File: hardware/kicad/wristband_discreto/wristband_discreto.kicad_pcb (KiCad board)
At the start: 2 copper layers, 32 x 32 mm, 24 parts, among them J1 Battery_Negative_Contact, U1 QFN-32-1EP_5x5mm_P0.5mm_EP3.6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, X1 Crystal_SMD_2016-4Pin_2.0x1.6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

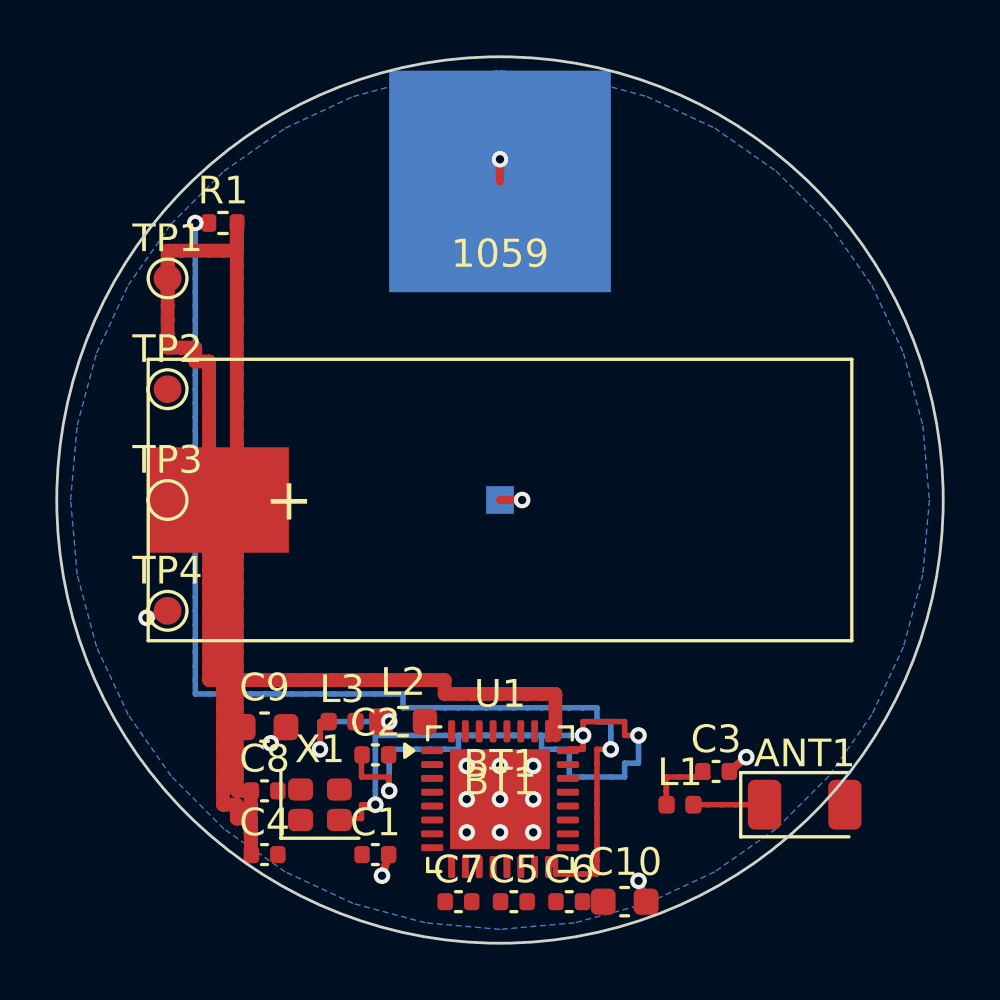
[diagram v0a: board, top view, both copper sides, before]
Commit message: Layouts finish, BM832A migration, fab package, quote, docs and status report
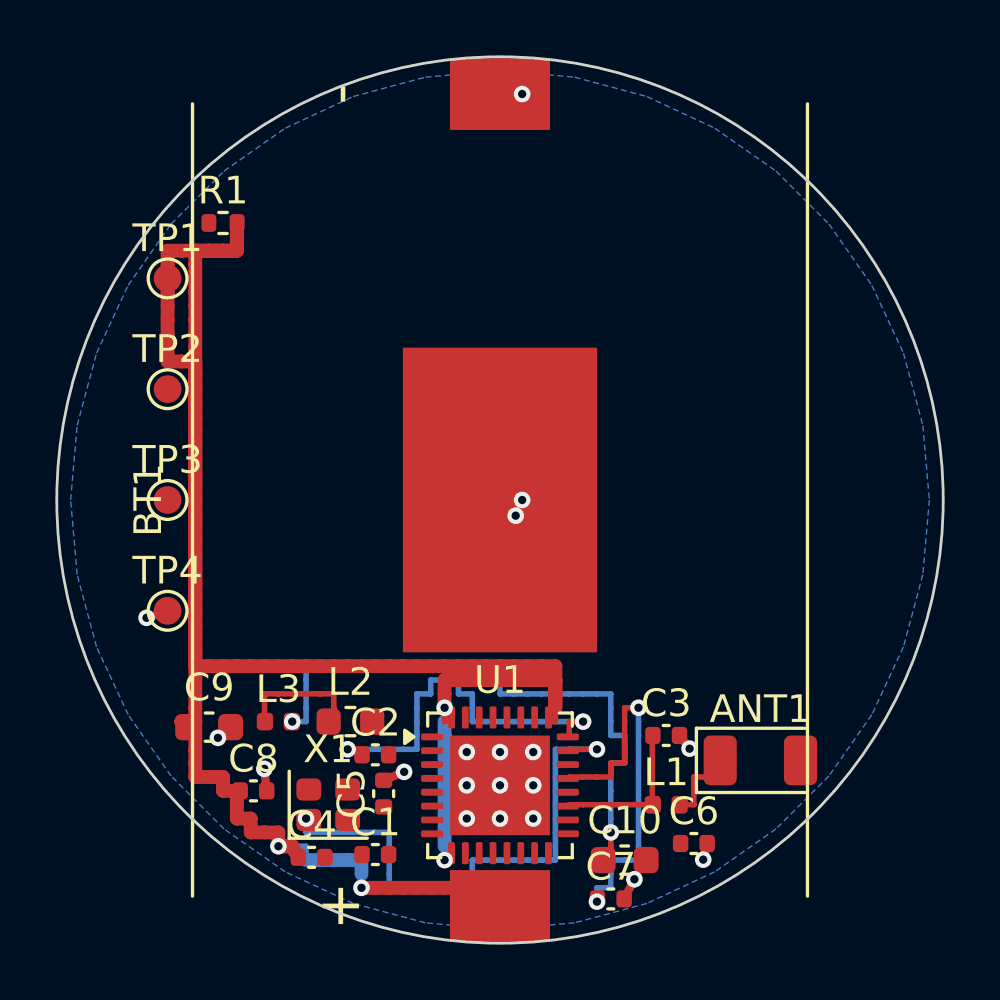
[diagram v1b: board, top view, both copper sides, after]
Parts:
- removed J1: Battery_Negative_Contact, J1_Battery_Negative_Contact
- BT1: value Keystone_1059 -> Keystone_1060; footprint Keystone_1059_CR2032_SMT -> Keystone_1060_CR2032_SMT
- moved C5 6.11 mm to (95.8, 110.6), turned to 90 degrees
- moved C7 5.50 mm to (104.0, 114.4)
- moved C6 4.97 mm to (107.0, 112.4)
- moved L3 2.30 mm to (92.0, 108.0)
- moved ANT1 2.26 mm to (109.4, 109.4)
- moved C3 2.22 mm to (106.0, 108.5)
- moved C9 2.00 mm to (89.5, 108.2)
- moved L2 1.90 mm to (94.6, 108.0)
- moved C4 1.70 mm to (93.2, 112.9)
- moved C10 1.50 mm to (104.5, 113.0)
- moved L1 0.50 mm to (106.0, 111.0)
- moved U1 0.50 mm to (100.0, 110.3)
- moved C8 0.40 mm to (91.1, 110.5)
- moved X1 0.30 mm to (93.8, 111.0)
- turned BT1 to -90 degrees
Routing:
- net NET_RESET: track 41.9 -> 0.00 mm, vias 2 -> 0
- net NET_DEC4: track 0.00 -> 22.2 mm, vias 0 -> 2
- net NET_XC2: track 34.0 -> 14.3 mm, vias 4 -> 2
- net NET_XC1: track 0.00 -> 19.2 mm, vias 0 -> 2
- net VDD_BAT: track 73.2 -> 89.9 mm, vias 0 -> 4
- net NET_DEC2: track 0.00 -> 13.7 mm, vias 0 -> 2
- net NET_ANT: track 2.78 -> 5.62 mm
- net GND: track 5.60 -> 7.40 mm, vias 16 -> 19
- net NET_L2_L3: track 5.90 -> 4.70 mm, vias 2 -> 0
- net NET_RF: track 2.56 -> 3.13 mm

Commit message: Manual routing discreta, module nudge, paho-mqtt 2.x, NVS provisioning, ANATEL scope fix
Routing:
- net NET_XC1: track 19.2 -> 47.2 mm, vias 2 -> 4
- net NET_DEC1: track 0.00 -> 4.40 mm
- net GND: track 7.40 -> 9.80 mm, vias 19 -> 22
